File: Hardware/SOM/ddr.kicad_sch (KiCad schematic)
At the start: 16 parts, among them U2 AS4C256M16D3

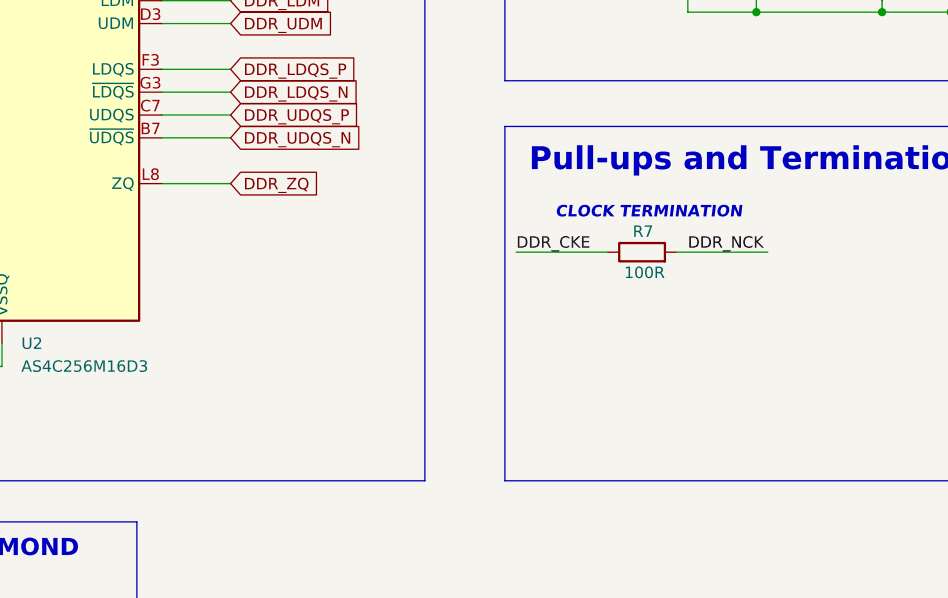
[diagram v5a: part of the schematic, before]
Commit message: ZQ calibration resistor added
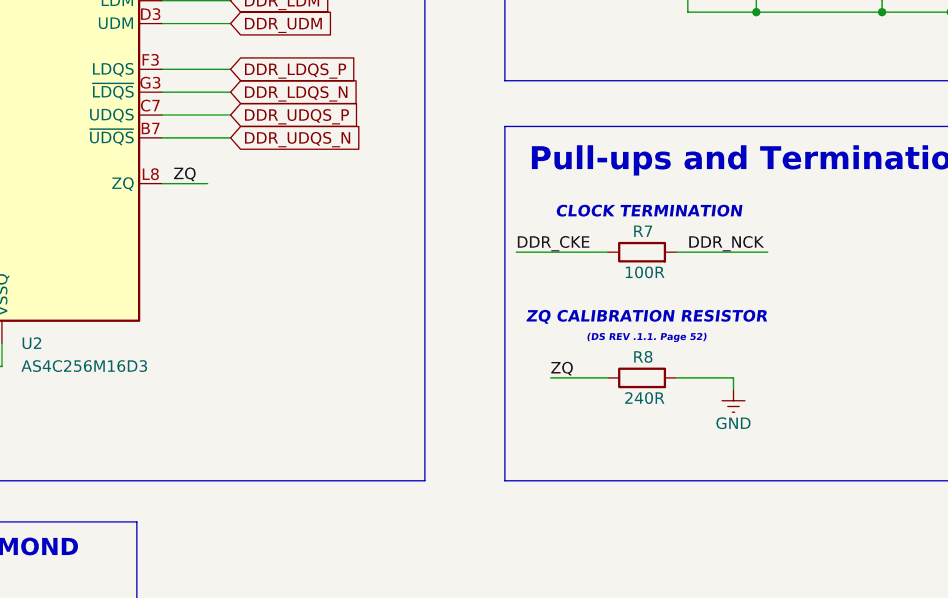
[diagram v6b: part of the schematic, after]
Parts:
- added R8: 240R, Resistor_SMD:R_0402_1005Metric, symbol Device:R
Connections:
- net GND: now also R8.2
- net DDR_ZQ renamed ZQ
- net ZQ: now also R8.1
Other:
- note added: "(DS REV .1.1. Page 52)"
- note added: "ZQ CALIBRATION RESISTOR"
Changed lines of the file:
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@@
 		)
 	)
+	(text "ZQ CALIBRATION RESISTOR"
+		(exclude_from_sim no)
+		(at 141.478 122.936 0)
+		(effects
+			(font
+				(size 1.27 1.27)
+				(thickness 0.254)
+				(bold yes)
+				(italic yes)
+				(color 0 132 0 1)
+			)
+		)
+	)
+	(text "(DS REV .1.1. Page 52)"
+		(exclude_from_sim no)
+		(at 141.478 125.222 0)
+		(effects
+			(font
+				(size 0.762 0.762)
+				(thickness 0.254)
+				(bold yes)
+				(italic yes)
+				(color 0 132 0 1)
+			)
+		)
+	)
 	(junction
 		(at 182.88 40.64)
@@
 	(wire
 		(pts
+			(xy 130.81 129.54) (xy 137.16 129.54)
+		)
+		(stroke
+			(width 0)
+			(type default)
+		)
+	)
+	(wire
+		(pts
 			(xy 182.88 40.64) (xy 182.88 41.91)
 		)
@@
 	(wire
 		(pts
-			(xy 87.63 107.95) (xy 95.25 107.95)
+			(xy 87.63 107.95) (xy 92.71 107.95)
 		)
 		(stroke
@@
 	(wire
 		(pts
+			(xy 151.13 129.54) (xy 144.78 129.54)
+		)
+		(stroke
+			(width 0)
+			(type default)
+		)
+	)
+	(wire
+		(pts
 			(xy 45.72 113.03) (xy 52.07 113.03)
 		)
@@
 	(wire
 		(pts
+			(xy 151.13 130.81) (xy 151.13 129.54)
+		)
+		(stroke
+			(width 0)
+			(type default)
+		)
+	)
+	(wire
+		(pts
 			(xy 153.67 88.9) (xy 146.05 88.9)
 		)
@@
 		)
 	)
+	(label "ZQ"
+		(at 130.81 129.54 0)
+		(effects
+			(font
+				(size 1.27 1.27)
+			)
+			(justify left bottom)
+		)
+	)
+	(label "ZQ"
+		(at 88.9 107.95 0)
+		(effects
+			(font
+				(size 1.27 1.27)
+			)
+			(justify left bottom)
+		)
+	)
 	(label "DDR_NCK"
 		(at 146.05 115.57 0)
@@
 		)
 	)
-	(global_label "DDR_ZQ"
-		(shape input)
-		(at 95.25 107.95 0)
-		(fields_autoplaced yes)
-		(effects
-			(font
-				(size 1.27 1.27)
-			)
-			(justify left)
-		)
-		(property "Intersheetrefs" "${INTERSHEET_REFS}"
-			(at 105.5528 107.95 0)
-			(effects
-				(font
-					(size 1.27 1.27)
-				)
-				(justify left)
-				(hide yes)
-			)
-		)
-	)
 	(global_label "DDR_DQ11"
 		(shape input)
@@
 	(symbol
 		(lib_id "power:GNDREF")
+		(at 151.13 130.81 0)
+		(unit 1)
+		(exclude_from_sim no)
+		(in_bom yes)
+		(on_board yes)
+		(dnp no)
+		(property "Reference" "#PWR034"
+			(at 151.13 137.16 0)
+			(effects
+				(font
+					(size 1.27 1.27)
+				)
+				(hide yes)
+			)
+		)
+		(property "Value" "GND"
+			(at 151.13 134.62 0)
+			(effects
+				(font
+					(size 1.27 1.27)
+				)
+			)
+		)
+		(property "Footprint" ""
+			(at 151.13 130.81 0)
+			(effects
+				(font
+					(size 1.27 1.27)
+				)
+				(hide yes)
+			)
+		)
+		(property "Datasheet" ""
+			(at 151.13 130.81 0)
+			(effects
+				(font
+					(size 1.27 1.27)
+				)
+				(hide yes)
+			)
+		)
+		(property "Description" "Power symbol creates a global label with name \"GNDREF\" , reference supply ground"
+			(at 151.13 130.81 0)
+			(effects
+				(font
+					(size 1.27 1.27)
+				)
+				(hide yes)
+			)
+		)
+		(pin "1"
+		)
+		(instances
+			(project "LFE5UM5G-85F_SOM"
+				(path "/de32abb0-ff3b-4c67-a91a-eed08140b1b2/70285655-daa5-4a1b-b29b-80c93a345d65"
+					(reference "#PWR034")
+					(unit 1)
+				)
+			)
+		)
+	)
+	(symbol
+		(lib_id "power:GNDREF")
 		(at 67.31 130.81 0)
 		(unit 1)
@@
 					(unit 1)
 				)
+			)
+		)
+	)
+	(symbol
+		(lib_id "Device:R")
+		(at 140.97 129.54 90)
+		(unit 1)
+		(exclude_from_sim no)
+		(in_bom yes)
+		(on_board yes)
+		(dnp no)
+		(property "Reference" "R8"
+			(at 142.24 127.254 90)
+			(effects
+				(font
+					(size 1.27 1.27)
+				)
+				(justify left)
+			)
+		)
+		(property "Value" "240R"
+			(at 143.51 131.826 90)
+			(effects
+				(font
+					(size 1.27 1.27)
+				)
+				(justify left)
+			)
+		)
+		(property "Footprint" "Resistor_SMD:R_0402_1005Metric"
+			(at 140.97 131.318 90)
+			(effects
+				(font
+					(size 1.27 1.27)
+				)
+				(hide yes)
+			)
+		)
+		(property "Datasheet" "~"
+			(at 140.97 129.54 0)
+			(effects
+				(font
+					(size 1.27 1.27)
+				)
+				(hide yes)
+			)
+		)
+		(property "Description" "Resistor"
+			(at 140.97 129.54 0)
+			(effects
+				(font
+					(size 1.27 1.27)
+				)
+				(hide yes)
+			)
+		)
+		(property "Manufacturer" "Würth Elektronik"
+			(at 140.97 129.54 0)
+			(effects
+				(font
+					(size 1.27 1.27)
+				)
+				(hide yes)
+			)
+		)
+		(property "MPN" "560112110009"
+			(at 140.97 129.54 0)
+			(effects
+				(font
+					(size 1.27 1.27)
+				)
+				(hide yes)
+			)
+		)
+		(pin "1"
+		)
+		(pin "2"
+		)
+		(instances
+			(project "LFE5UM5G-85F_SOM"
+				(path "/de32abb0-ff3b-4c67-a91a-eed08140b1b2/70285655-daa5-4a1b-b29b-80c93a345d65"
+					(reference "R8")
+					(unit 1)
+				)

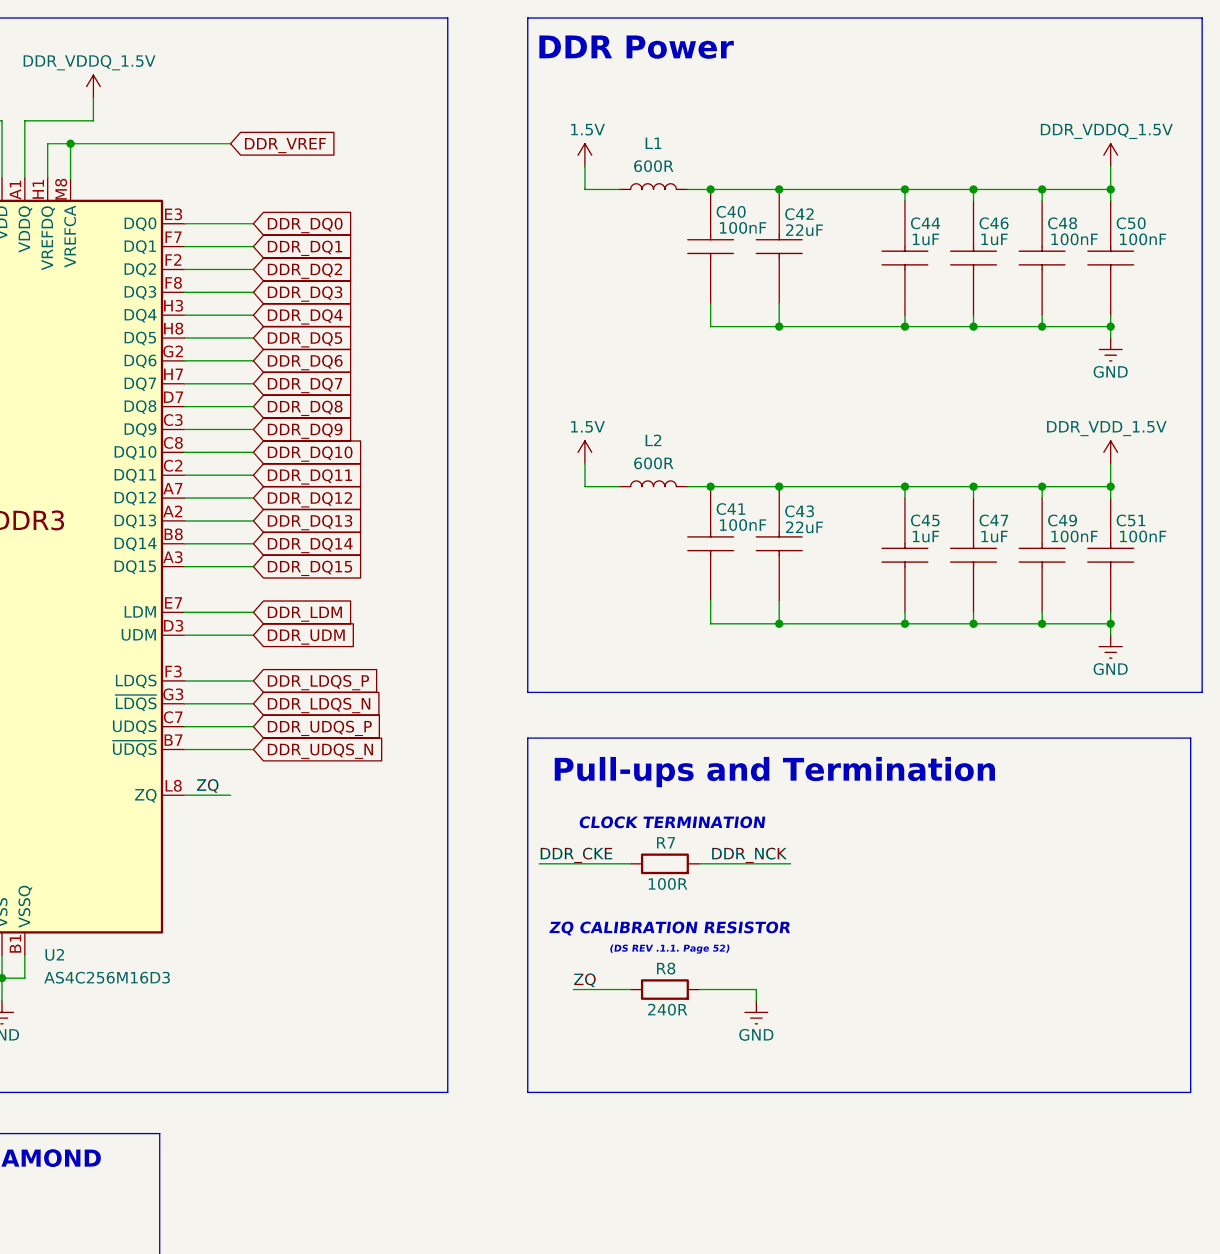
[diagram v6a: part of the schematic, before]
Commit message: SOM: Boot mode CFG
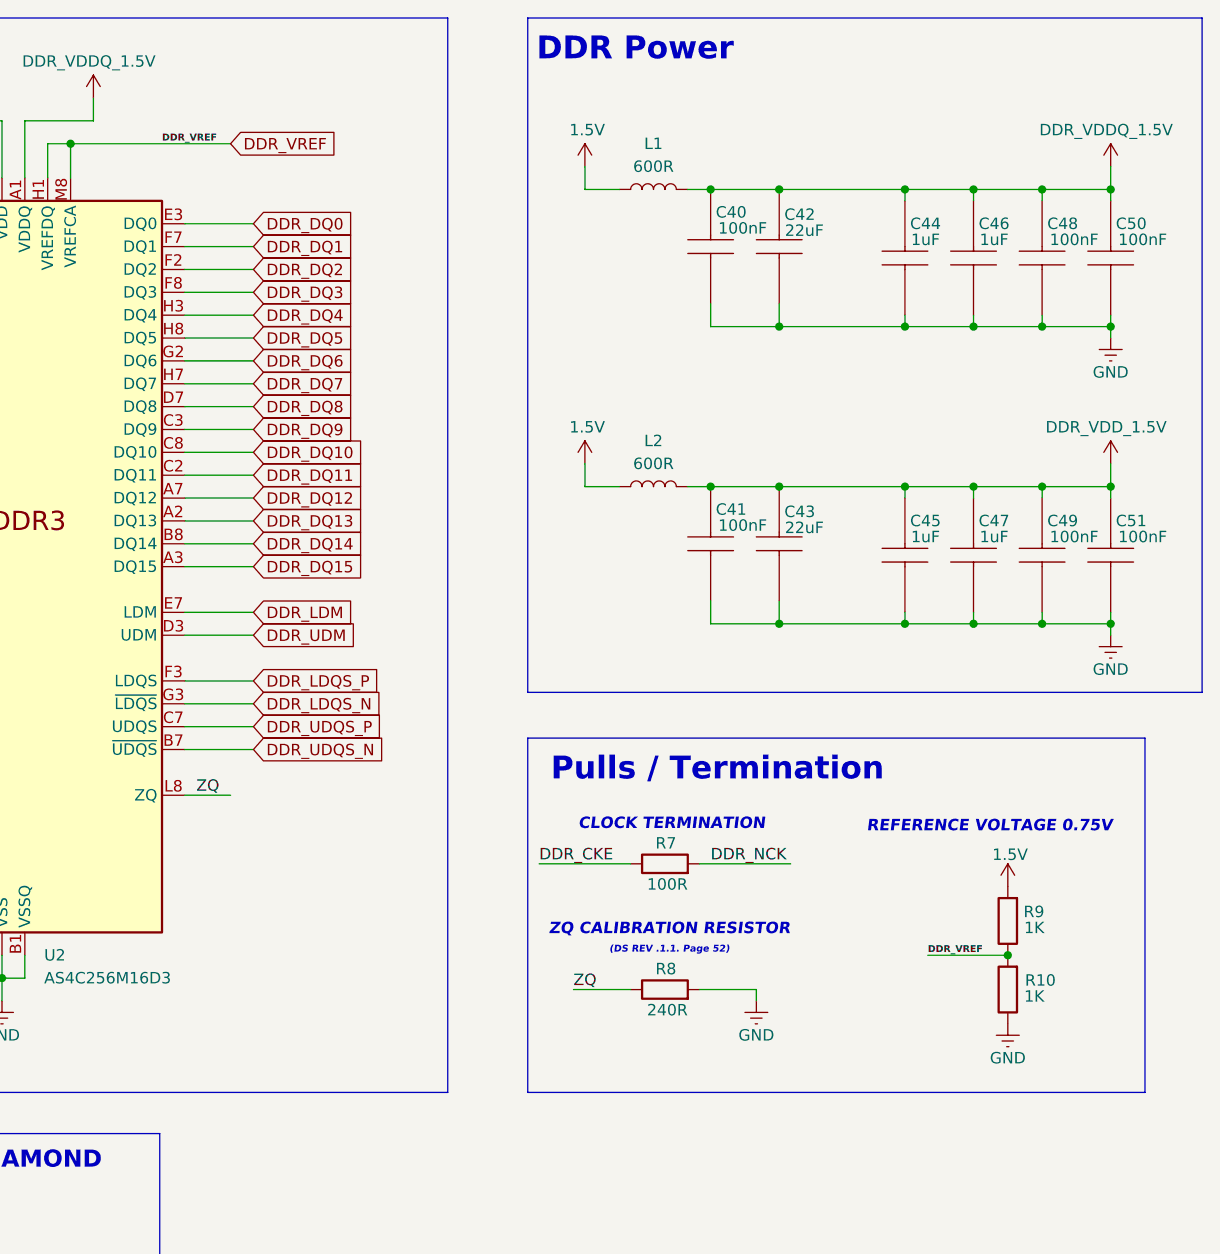
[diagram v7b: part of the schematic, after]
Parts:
- added R10, R9: 1K, Resistor_SMD:R_0402_1005Metric, symbol Device:R
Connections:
- net 1.5V: now also R9.2
- net DDR_VREF: now also R10.2, R9.1
- net GND: now also R10.1
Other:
- note added: "Pulls / Termination"
- note added: "REFERENCE VOLTAGE 0.75V"
- note removed: "Pull-ups and Termination"

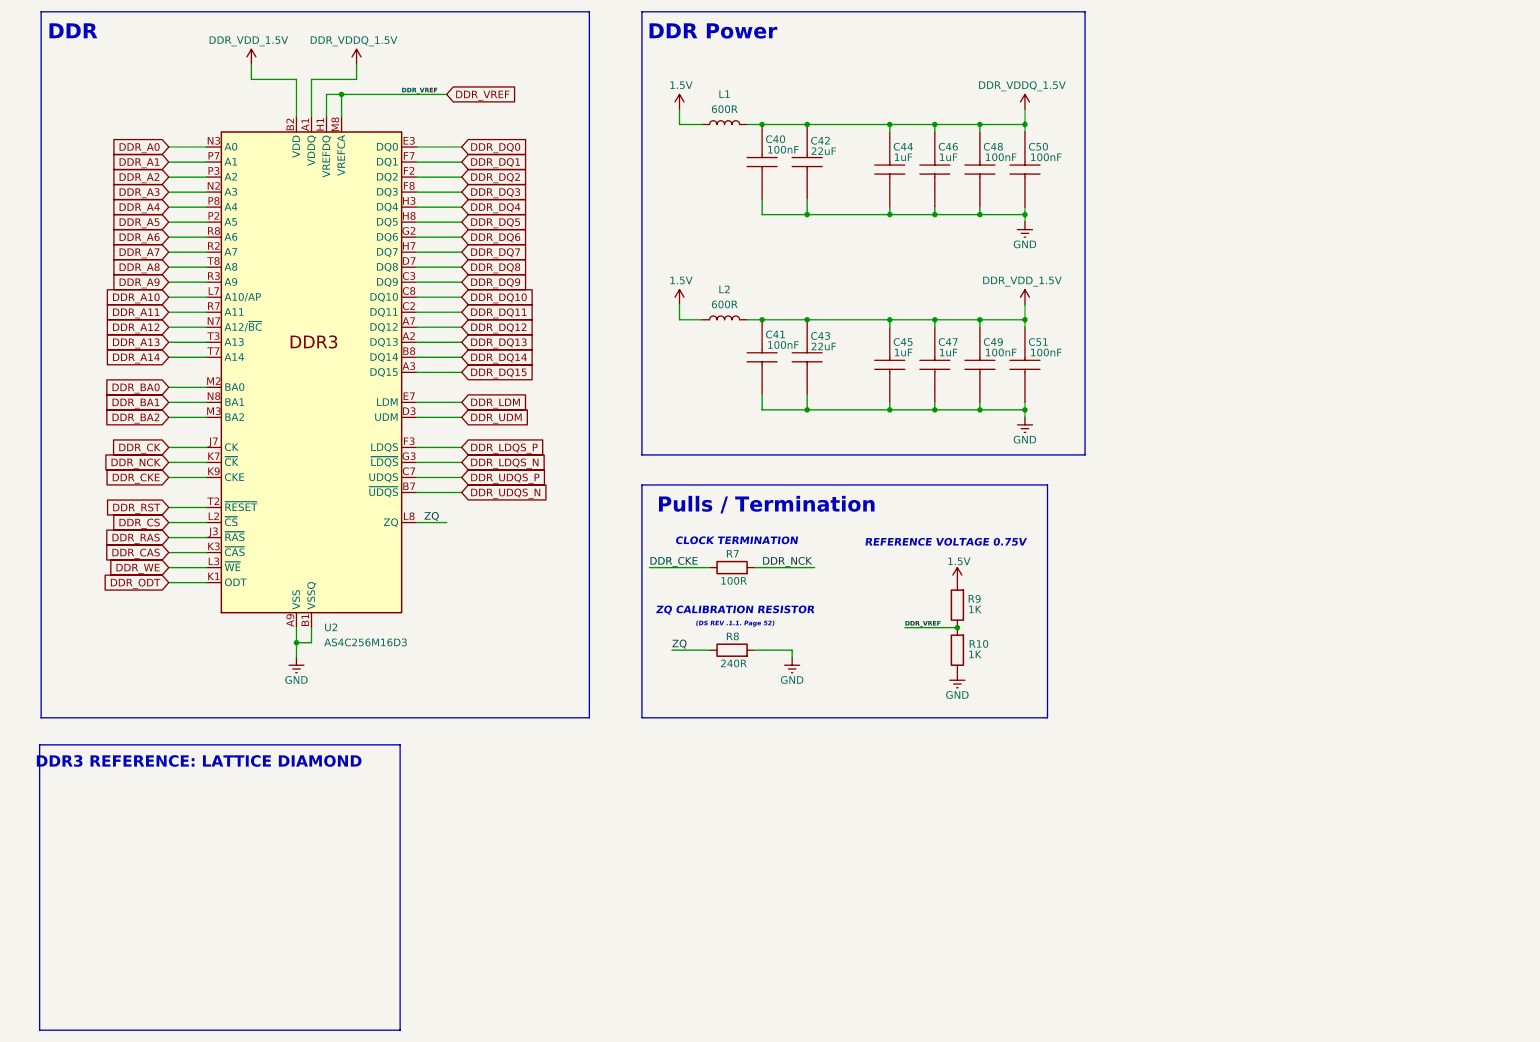
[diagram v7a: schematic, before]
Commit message: SOM: DDR pull-ups
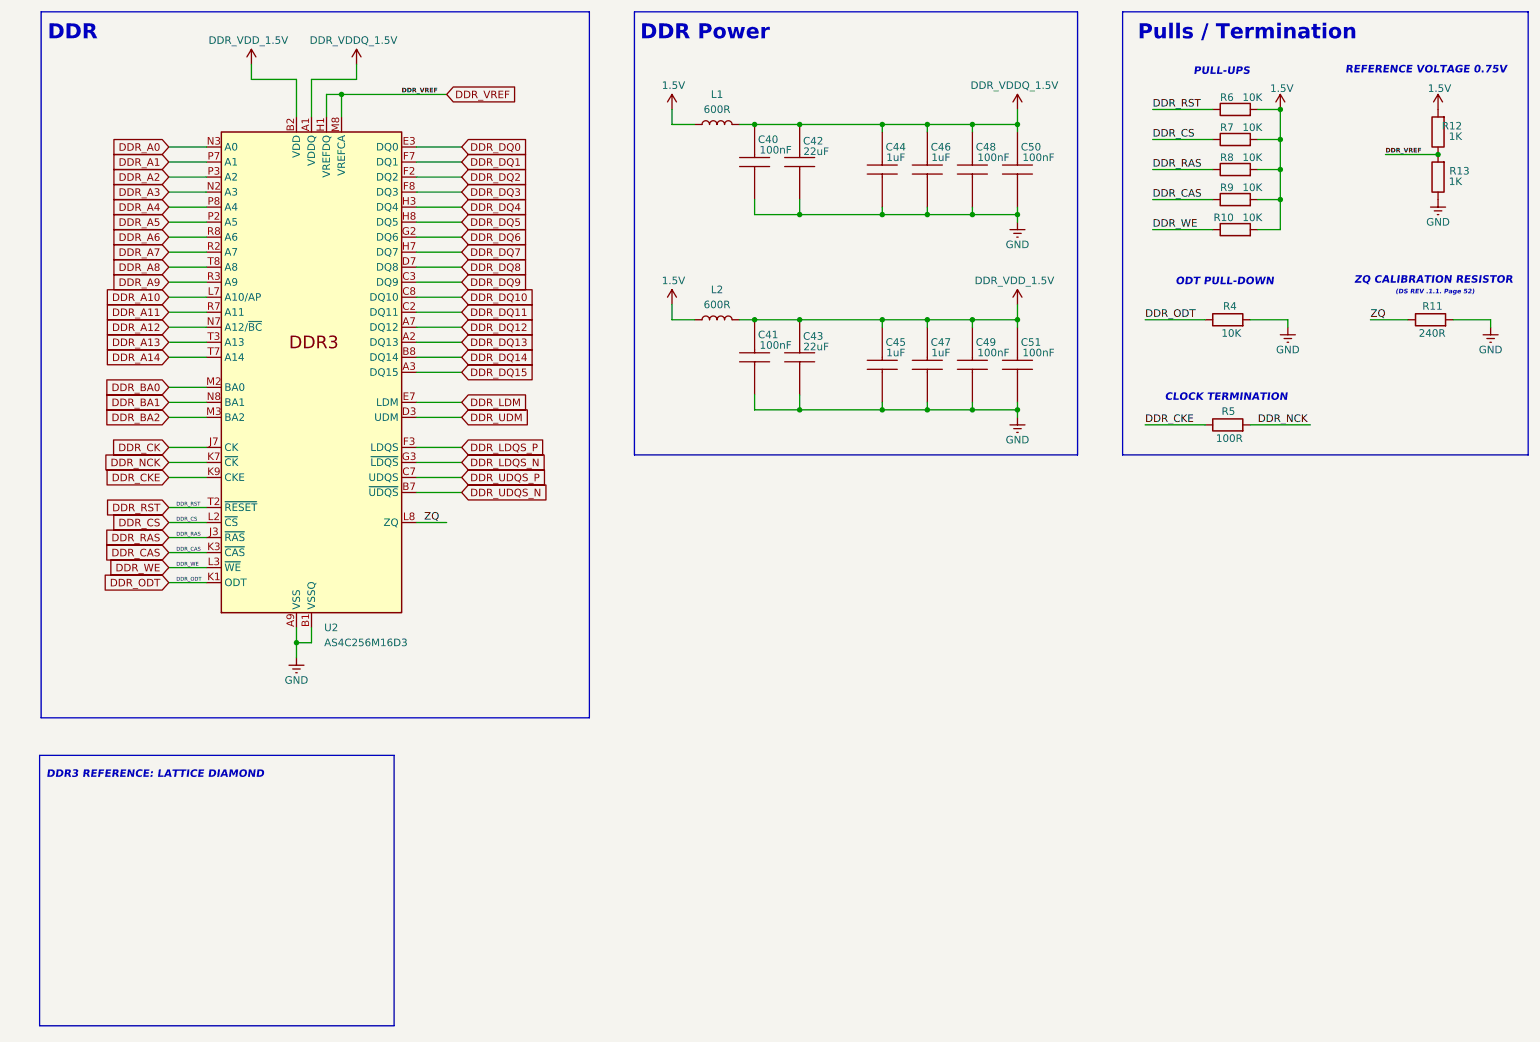
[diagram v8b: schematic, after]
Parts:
- added R10, R4, R6, R7, R8, R9: 10K, Resistor_SMD:R_0402_1005Metric, symbol Device:R
- renumbered R8 to R11, R9 to R12, R10 to R13, R7 to R5
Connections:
- net 1.5V: now also R10.2, R6.2, R7.2, R8.2, R9.2
- net DDR_CAS: now also R9.1
- net DDR_CS: now also R7.1
- net DDR_ODT: now also R4.1
- net DDR_RAS: now also R8.1
- net DDR_RST: now also R6.1
- net DDR_WE: now also R10.1
- net GND: now also R4.2
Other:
- note added: "ODT PULL-DOWN"
- note added: "PULL-UPS"
- moved on the sheet: C40, C41, C42, C43, C44, C45, C46, C47, C48, C49, C50, C51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
